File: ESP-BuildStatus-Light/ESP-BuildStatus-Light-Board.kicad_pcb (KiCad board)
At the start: 2 copper layers, 113 x 126.6 mm, 61 parts, among them J2 CONN_01X16, SW1 SW_Push, U1 APA102C, U10 APA102C, U11 APA102C, U12 APA102C, U13 APA102C, U14 APA102C, U15 APA102C, U16 APA102C, U17 APA102C, U18 APA102C, U19 APA102C, U2 APA102C, U20 APA102C, U21 APA102C, U22 APA102C, U23 APA102C, U24 APA102C, U25 APA102C, U26 APA102C, U27 APA102C, U28 APA102C, U29 APA102C, U3 APA102C, U30 APA102C, U31 APA102C, U32 APA102C, U33 APA102C, U34 APA102C, U35 APA102C, U36 APA102C, U37 APA102C, U38 APA102C, U39 APA102C, U4 APA102C, U40 APA102C, U41 APA102C, U42 APA102C, U43 APA102C, U44 APA102C, U45 APA102C, U46 APA102C, U47 APA102C, U48 APA102C, U49 APA102C, U5 APA102C, U50 WeMos_mini, U51 74HCT541_PWR, U6 APA102C, U7 APA102C, U8 APA102C, U9 APA102C

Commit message: Modified traces from WeMos to Level Shifter
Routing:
- net Net-(SW1-Pad1): track 133.0 -> 170.2 mm, vias 0 -> 2
- net Net-(U50-Pad15): track 115.2 -> 141.5 mm
- net Net-(U50-Pad13): track 121.4 -> 139.2 mm
- net GND: track 104.5 -> 120.8 mm, vias 53 -> 55
- net Net-(U50-Pad11): track 128.5 -> 136.0 mm
- net Net-(U50-Pad6): track 110.3 -> 114.8 mm
- net Net-(U50-Pad5): track 106.5 -> 110.3 mm
- net Net-(U1-Pad2): track 177.7 -> 176.6 mm
- net Net-(U50-Pad3): track 105.6 -> 106.4 mm
- net Net-(J2-Pad4): track 11.2 -> 12.0 mm

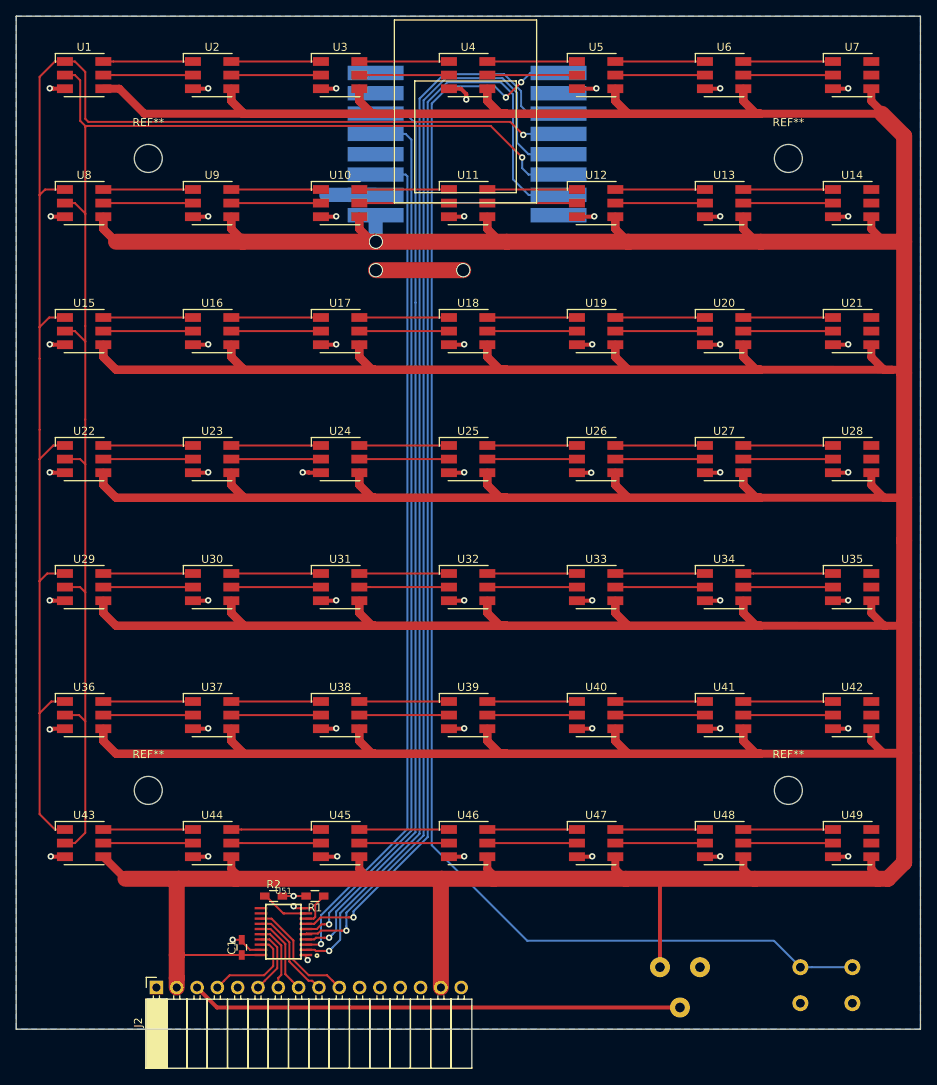
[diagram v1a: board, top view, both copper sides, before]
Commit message: Updated the traces between ESP and LCD for better grounding
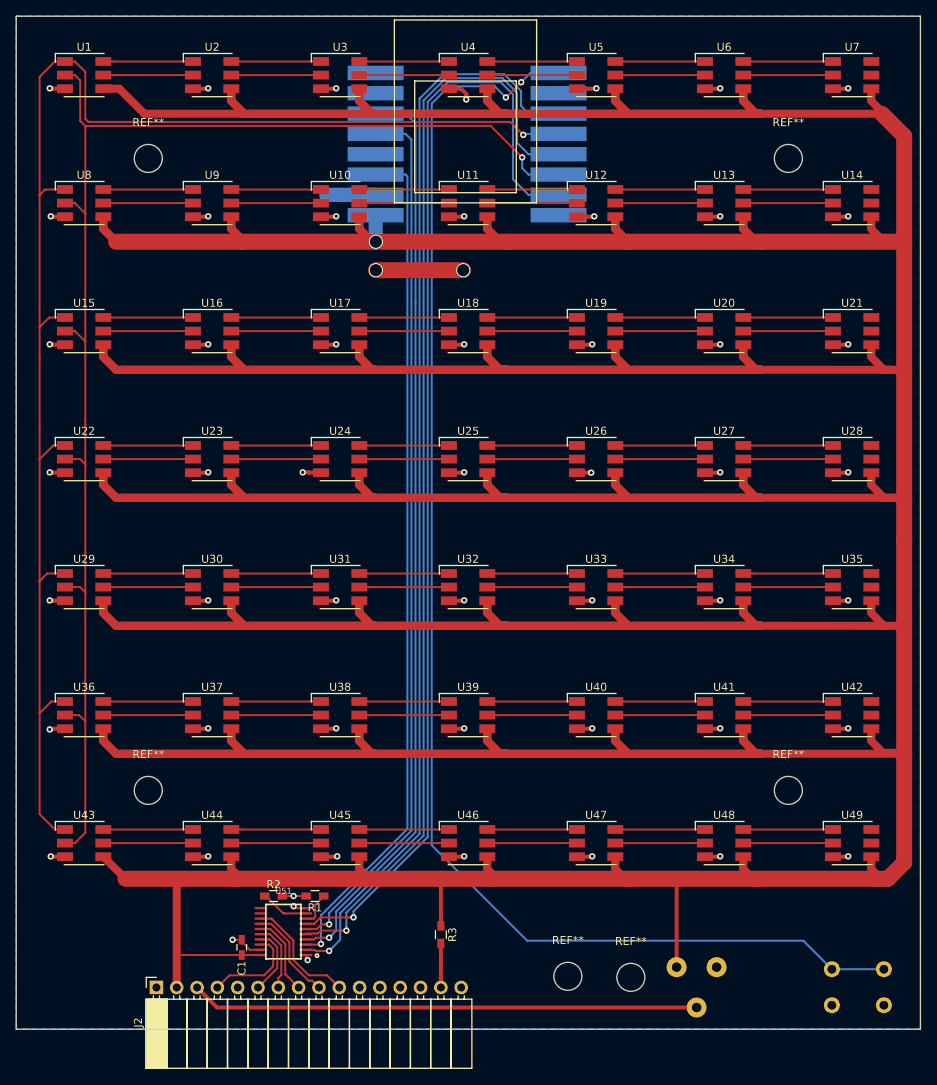
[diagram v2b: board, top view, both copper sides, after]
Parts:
- added R3: 1K, Resistors_SMD:R_0603_HandSoldering, F.Cu at (183.5, 133.1)
- added REF**: MountingHole_3.5mm, Mounting_Holes:MountingHole_3.5mm, F.Cu at (199.4, 138.3)
- added REF**: MountingHole_3.5mm, Mounting_Holes:MountingHole_3.5mm, F.Cu at (207.3, 138.4)
- moved SW1 3.95 mm to (238.9, 137.4)
- moved RV1 2.08 mm to (213.0, 137.2)
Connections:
- J2 pad 15: +5V -> Net-(J2-Pad15)
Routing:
- net +5V: track 1567.0 -> 1559.6 mm
- net Net-(J2-Pad15): track 0.00 -> 5.50 mm
- net Net-(SW1-Pad1): track 170.2 -> 174.2 mm
- net Net-(J2-Pad3): track 61.4 -> 63.5 mm
